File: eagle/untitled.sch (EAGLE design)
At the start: 29 parts, among them K1 AZ8-FORM-A, Q1 IRFZ24NPBF, U1 ATTINY85-20S, X1 MKDSN1,5/3-5,08, X2 MKDSN1,5/3-5,08

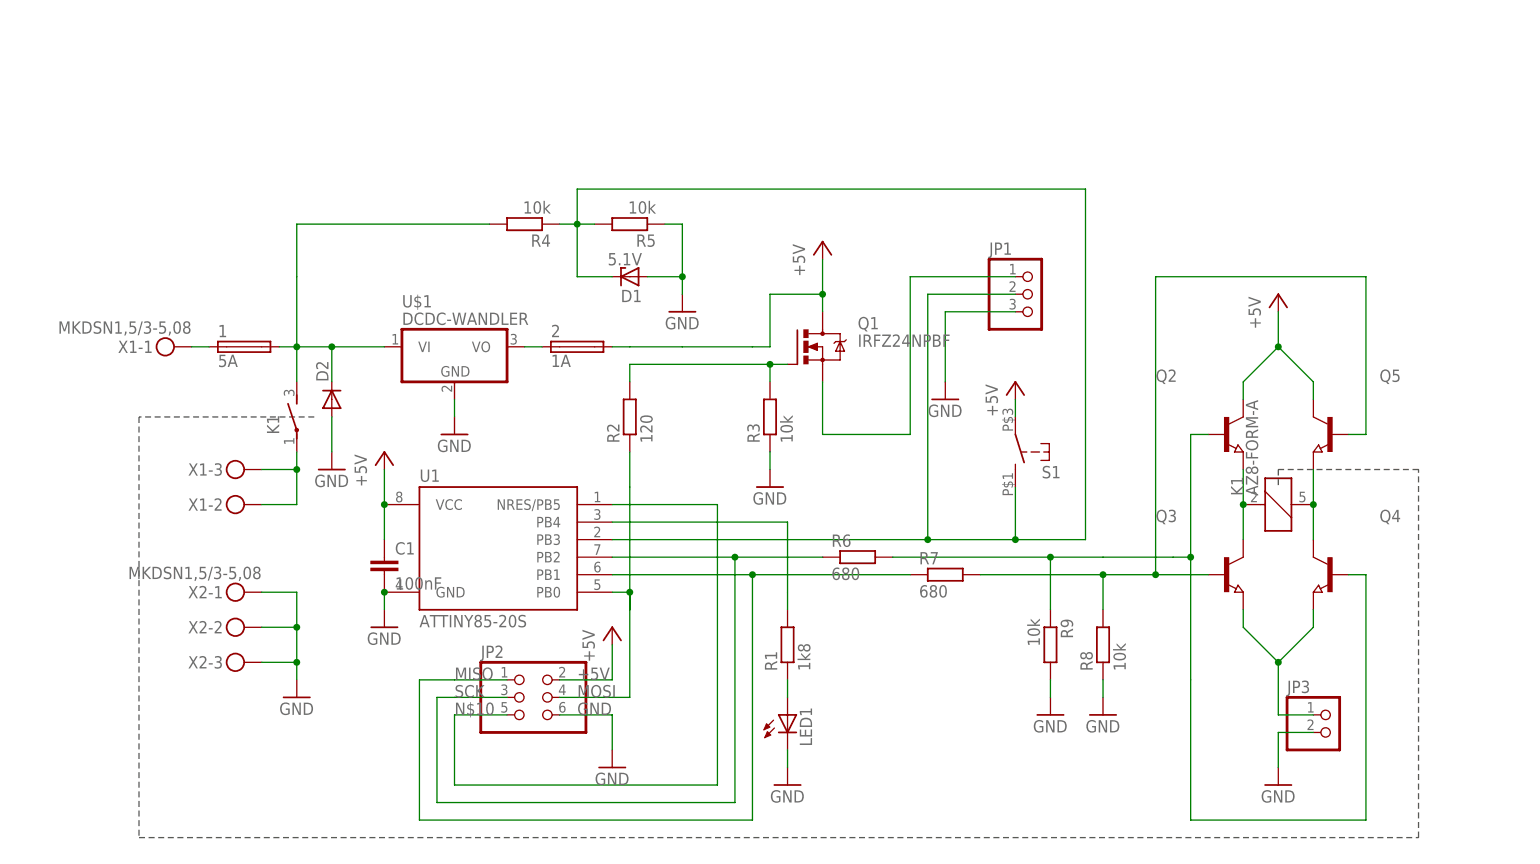
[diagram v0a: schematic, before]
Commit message: Added resistor for npn transistors
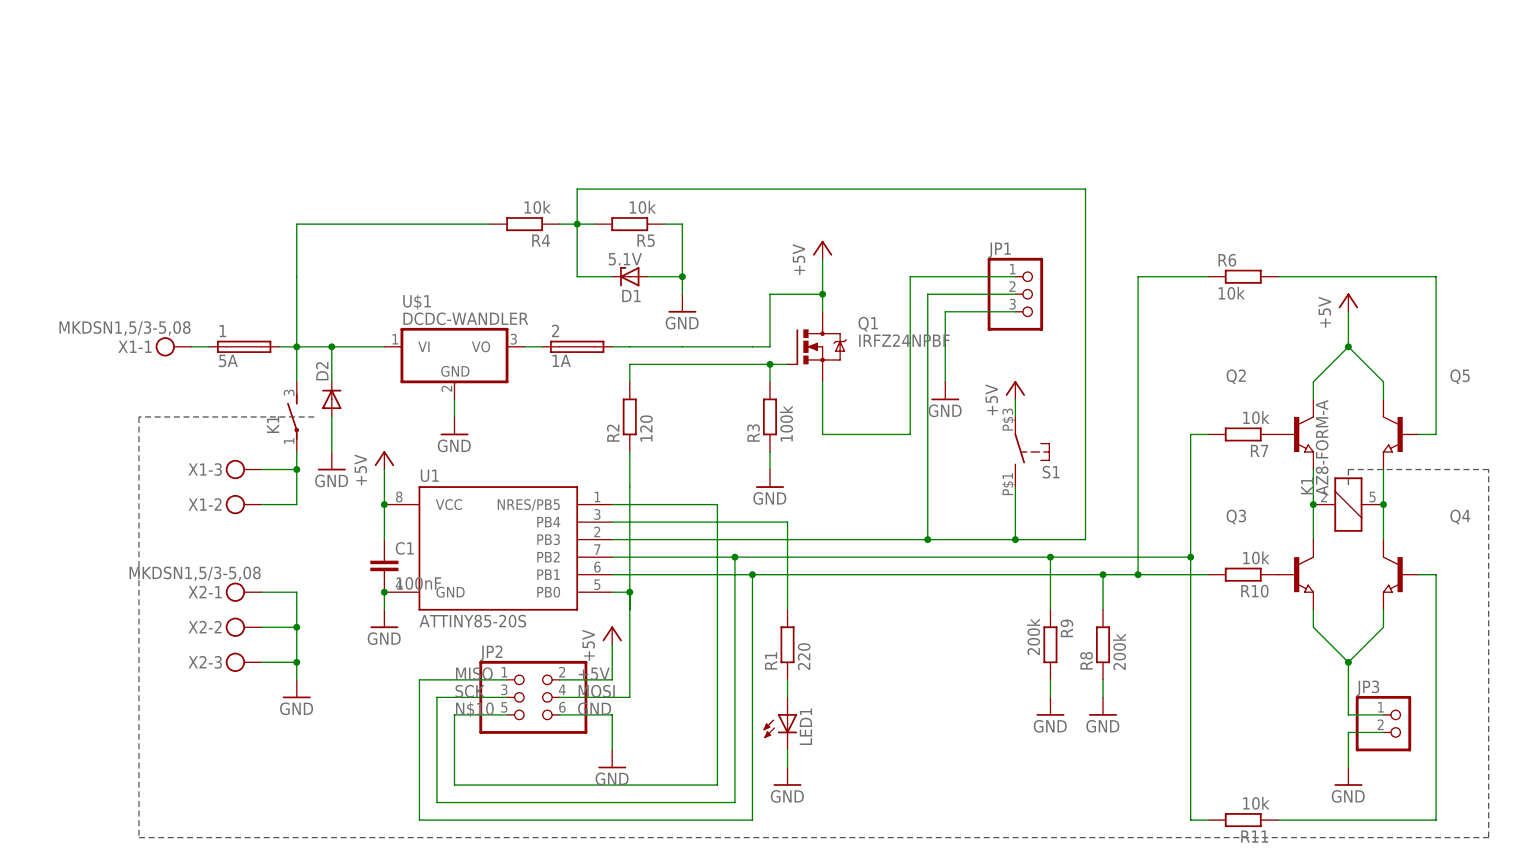
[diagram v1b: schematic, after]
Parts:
- added R10, R11: 10k, rcl:R-EU_R1206
- R1: value 1k8 -> 220
- R3: value 10k -> 100k
- R6, R7: value 680 -> 10k
- R8, R9: value 10k -> 200k
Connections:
- removed net N$16: Q3.B, Q5.B, R7.2, R8.2
- removed net N$17: Q2.B, Q4.B, R6.2, R9.1
- new net N$14: Q5.B, R6.2
- new net N$15: Q2.B, R7.1
- new net N$19: Q3.B, R10.1
- new net N$20: Q4.B, R11.1
- net MISO: now also R10.2, R6.1, R8.2; no longer R7.1
- net SCK: now also R11.2, R7.2, R9.1; no longer R6.1
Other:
- moved on the sheet: JP3, K1, Q2, Q3, Q4, Q5, R6, R7

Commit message: Pullup- reset & 2x voltage divider
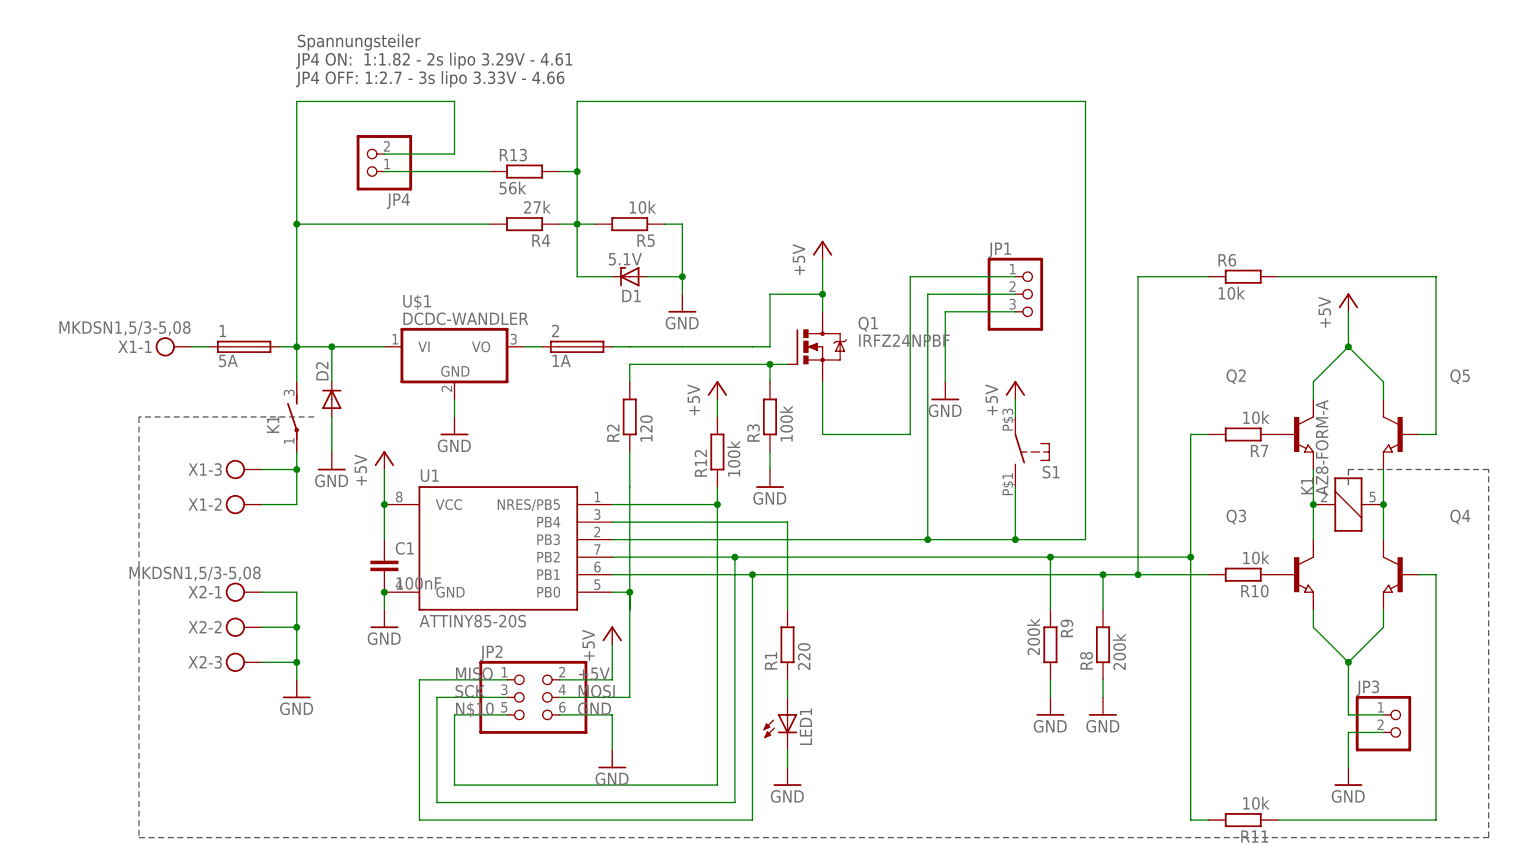
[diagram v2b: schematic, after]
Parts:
- added JP4: (no value), pinhead:PINHD-1X2
- added R12: 100k, rcl:R-EU_R1206
- added R13: 56k, rcl:R-EU_R1206
- R4: value 10k -> 27k
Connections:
- new net N$16: JP4.1, R13.1
- net +5V: now also R12.2
- net N$10: now also R12.1
- net N$2: now also JP4.2
- net RESET: now also R13.2
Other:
- note added: "Spannungsteiler JP4 ON: 1:1.82 - 2s lipo 3.29V - 4.61 JP4 OFF: 1:2.7 - 3s lipo 3.33V - 4.66"
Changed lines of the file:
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@@
 <part name="GND4" library="supply1" deviceset="GND" device=""/>
 <part name="JP1" library="pinhead" deviceset="PINHD-1X3" device=""/>
-<part name="R4" library="rcl" deviceset="R-EU_" device="R1206" value="10k"/>
+<part name="R4" library="rcl" deviceset="R-EU_" device="R1206" value="27k"/>
 <part name="R5" library="rcl" deviceset="R-EU_" device="R1206" value="10k"/>
 <part name="GND6" library="supply1" deviceset="GND" device=""/>
@@
 <part name="R10" library="rcl" deviceset="R-EU_" device="R1206" value="10k"/>
 <part name="R11" library="rcl" deviceset="R-EU_" device="R1206" value="10k"/>
+<part name="P+6" library="supply1" deviceset="+5V" device=""/>
+<part name="R12" library="rcl" deviceset="R-EU_" device="R1206" value="100k"/>
+<part name="JP4" library="pinhead" deviceset="PINHD-1X2" device=""/>
+<part name="R13" library="rcl" deviceset="R-EU_" device="R1206" value="56k"/>
 </parts>
 <sheets>
@@
 <wire x1="170.18" y1="71.12" x2="149.86" y2="71.12" width="0.1524" layer="97" style="shortdash"/>
 <wire x1="149.86" y1="71.12" x2="149.86" y2="68.58" width="0.1524" layer="97" style="shortdash"/>
+<text x="-2.54" y="127" size="1.778" layer="97">Spannungsteiler
+JP4 ON:  1:1.82 - 2s lipo 3.29V - 4.61
+JP4 OFF: 1:2.7 - 3s lipo 3.33V - 4.66</text>
 </plain>
 <instances>
@@
 <instance part="R10" gate="G$1" x="134.62" y="55.88" rot="R180"/>
 <instance part="R11" gate="G$1" x="134.62" y="20.32" rot="R180"/>
+<instance part="P+6" gate="1" x="58.42" y="83.82"/>
+<instance part="R12" gate="G$1" x="58.42" y="73.66" rot="R90"/>
+<instance part="JP4" gate="G$1" x="7.62" y="116.84" rot="R180"/>
+<instance part="R13" gate="G$1" x="30.48" y="114.3"/>
 </instances>
 <busses>
@@
 <pinref part="R4" gate="G$1" pin="2"/>
 <wire x1="-2.54" y1="106.68" x2="25.4" y2="106.68" width="0.1524" layer="91"/>
-<wire x1="-2.54" y1="99.06" x2="-2.54" y2="106.68" width="0.1524" layer="91"/>
 <pinref part="U$1" gate="G$1" pin="VI"/>
 <wire x1="-2.54" y1="88.9" x2="2.54" y2="88.9" width="0.1524" layer="91"/>
 <wire x1="2.54" y1="88.9" x2="10.16" y2="88.9" width="0.1524" layer="91"/>
-<wire x1="-2.54" y1="88.9" x2="-2.54" y2="99.06" width="0.1524" layer="91"/>
+<wire x1="-2.54" y1="88.9" x2="-2.54" y2="106.68" width="0.1524" layer="91"/>
 <junction x="-2.54" y="88.9"/>
 <pinref part="1" gate="G$1" pin="2"/>
@@
 <wire x1="2.54" y1="83.82" x2="2.54" y2="88.9" width="0.1524" layer="91"/>
 <junction x="2.54" y="88.9"/>
+<wire x1="-2.54" y1="106.68" x2="-2.54" y2="124.46" width="0.1524" layer="91"/>
+<junction x="-2.54" y="106.68"/>
+<wire x1="-2.54" y1="124.46" x2="20.32" y2="124.46" width="0.1524" layer="91"/>
+<wire x1="20.32" y1="124.46" x2="20.32" y2="116.84" width="0.1524" layer="91"/>
+<pinref part="JP4" gate="G$1" pin="2"/>
+<wire x1="20.32" y1="116.84" x2="10.16" y2="116.84" width="0.1524" layer="91"/>
 </segment>
 </net>
@@
 <wire x1="35.56" y1="106.68" x2="38.1" y2="106.68" width="0.1524" layer="91"/>
 <wire x1="38.1" y1="106.68" x2="40.64" y2="106.68" width="0.1524" layer="91"/>
-<wire x1="38.1" y1="106.68" x2="38.1" y2="111.76" width="0.1524" layer="91"/>
+<wire x1="38.1" y1="106.68" x2="38.1" y2="114.3" width="0.1524" layer="91"/>
 <junction x="38.1" y="106.68"/>
-<wire x1="38.1" y1="111.76" x2="111.76" y2="111.76" width="0.1524" layer="91"/>
+<wire x1="38.1" y1="114.3" x2="38.1" y2="124.46" width="0.1524" layer="91"/>
+<wire x1="38.1" y1="124.46" x2="111.76" y2="124.46" width="0.1524" layer="91"/>
 <pinref part="U1" gate="G$1" pin="PB3"/>
 <wire x1="43.18" y1="60.96" x2="88.9" y2="60.96" width="0.1524" layer="91"/>
 <wire x1="88.9" y1="60.96" x2="101.6" y2="60.96" width="0.1524" layer="91"/>
 <wire x1="101.6" y1="60.96" x2="111.76" y2="60.96" width="0.1524" layer="91"/>
-<wire x1="111.76" y1="60.96" x2="111.76" y2="111.76" width="0.1524" layer="91"/>
+<wire x1="111.76" y1="60.96" x2="111.76" y2="124.46" width="0.1524" layer="91"/>
 <pinref part="JP1" gate="A" pin="2"/>
 <wire x1="101.6" y1="96.52" x2="88.9" y2="96.52" width="0.1524" layer="91"/>
@@
 <wire x1="101.6" y1="68.58" x2="101.6" y2="60.96" width="0.1524" layer="91"/>
 <junction x="101.6" y="60.96"/>
+<pinref part="R13" gate="G$1" pin="2"/>
+<wire x1="38.1" y1="114.3" x2="35.56" y2="114.3" width="0.1524" layer="91"/>
+<junction x="38.1" y="114.3"/>
 </segment>
 </net>
@@
 <wire x1="66.04" y1="96.52" x2="73.66" y2="96.52" width="0.1524" layer="91"/>
 <junction x="73.66" y="96.52"/>
+</segment>
+<segment>
+<pinref part="P+6" gate="1" pin="+5V"/>
+<pinref part="R12" gate="G$1" pin="2"/>
+<wire x1="58.42" y1="81.28" x2="58.42" y2="78.74" width="0.1524" layer="91"/>
 </segment>
 </net>
@@
 <wire x1="20.32" y1="25.4" x2="58.42" y2="25.4" width="0.1524" layer="91"/>
 <label x="20.32" y="35.56" size="1.778" layer="95"/>
+<pinref part="R12" gate="G$1" pin="1"/>
+<wire x1="58.42" y1="68.58" x2="58.42" y2="66.04" width="0.1524" layer="91"/>
+<junction x="58.42" y="66.04"/>
 </segment>
 </net>
@@
 </segment>
 </net>
+<net name="N$16" class="0">
+<segment>
+<pinref part="R13" gate="G$1" pin="1"/>
+<pinref part="JP4" gate="G$1" pin="1"/>
+<wire x1="25.4" y1="114.3" x2="10.16" y2="114.3" width="0.1524" layer="91"/>
+</segment>
+</net>
 </nets>
 </sheet>
@@
 </schematic>
 </drawing>
+<compatibility>
+<note version="6.3" minversion="6.2.2" severity="warning">
+Since Version 6.2.2 text objects can contain more than one line,
+which will not be processed correctly with this version.
+</note>
+</compatibility>
 </eagle>

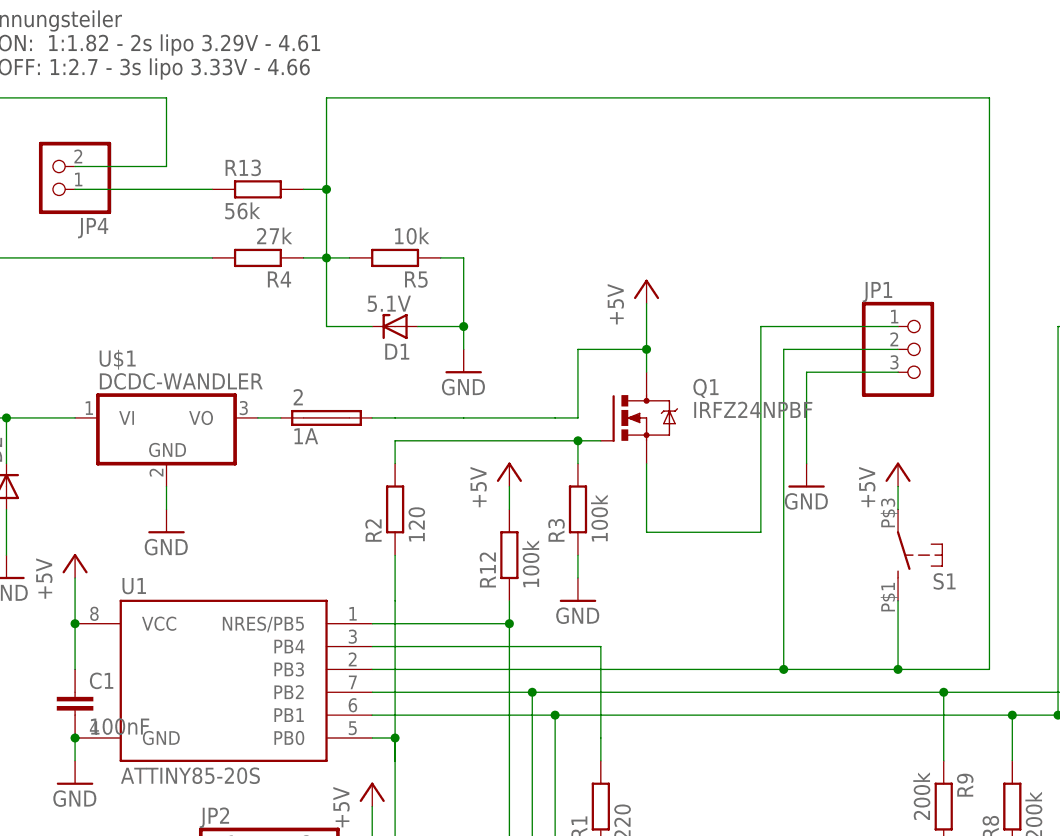
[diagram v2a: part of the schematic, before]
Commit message: Additional jumper for 2s and 3s lipo battery
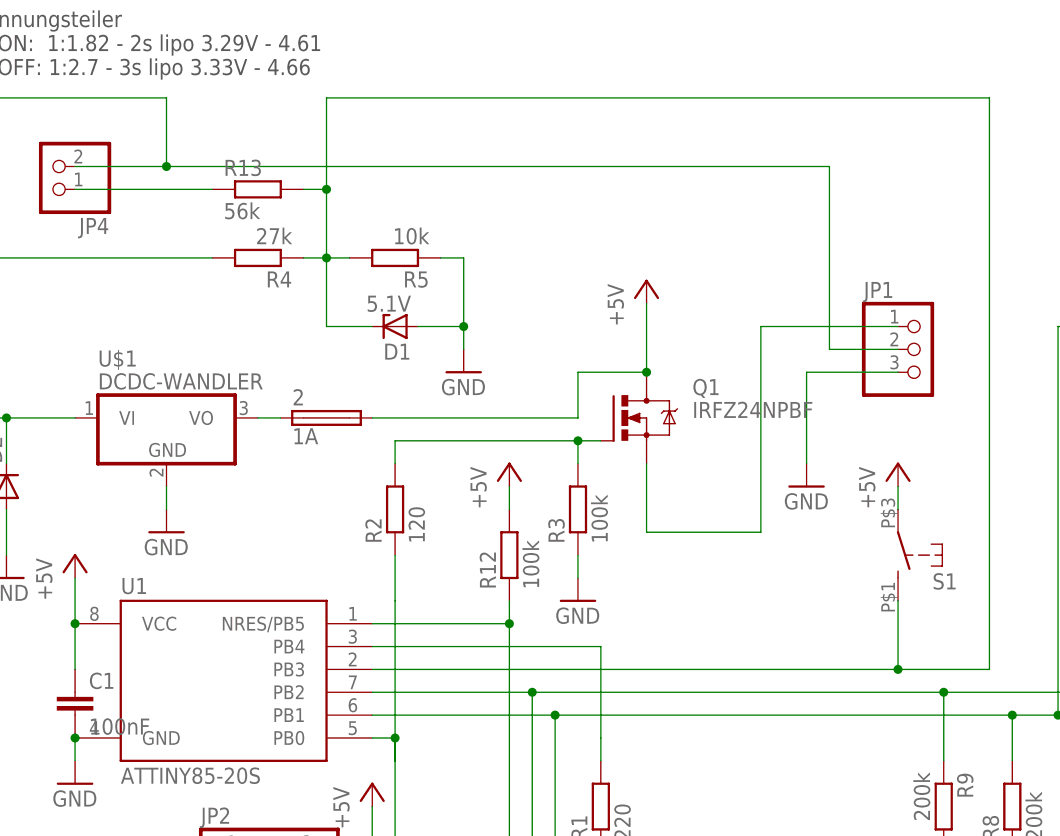
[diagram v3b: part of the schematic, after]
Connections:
- net N$2: now also JP1.2
- net RESET: no longer JP1.2
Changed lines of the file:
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@@
 <pinref part="JP4" gate="G$1" pin="2"/>
 <wire x1="20.32" y1="116.84" x2="10.16" y2="116.84" width="0.1524" layer="91"/>
+<junction x="20.32" y="116.84"/>
+<wire x1="20.32" y1="116.84" x2="93.98" y2="116.84" width="0.1524" layer="91"/>
+<wire x1="93.98" y1="116.84" x2="93.98" y2="96.52" width="0.1524" layer="91"/>
+<pinref part="JP1" gate="A" pin="2"/>
+<wire x1="93.98" y1="96.52" x2="101.6" y2="96.52" width="0.1524" layer="91"/>
 </segment>
 </net>
@@
 <wire x1="38.1" y1="124.46" x2="111.76" y2="124.46" width="0.1524" layer="91"/>
 <pinref part="U1" gate="G$1" pin="PB3"/>
-<wire x1="43.18" y1="60.96" x2="88.9" y2="60.96" width="0.1524" layer="91"/>
-<wire x1="88.9" y1="60.96" x2="101.6" y2="60.96" width="0.1524" layer="91"/>
+<wire x1="43.18" y1="60.96" x2="101.6" y2="60.96" width="0.1524" layer="91"/>
 <wire x1="101.6" y1="60.96" x2="111.76" y2="60.96" width="0.1524" layer="91"/>
 <wire x1="111.76" y1="60.96" x2="111.76" y2="124.46" width="0.1524" layer="91"/>
-<pinref part="JP1" gate="A" pin="2"/>
-<wire x1="101.6" y1="96.52" x2="88.9" y2="96.52" width="0.1524" layer="91"/>
-<wire x1="88.9" y1="96.52" x2="88.9" y2="60.96" width="0.1524" layer="91"/>
-<junction x="88.9" y="60.96"/>
 <wire x1="38.1" y1="106.68" x2="38.1" y2="99.06" width="0.1524" layer="91"/>
 <pinref part="D1" gate="G$1" pin="C"/>
@@
 </segment>
 <segment>
-<wire x1="43.18" y1="88.9" x2="45.72" y2="88.9" width="0.1524" layer="91"/>
-<wire x1="45.72" y1="88.9" x2="53.34" y2="88.9" width="0.1524" layer="91"/>
 <pinref part="Q1" gate="G$1" pin="D"/>
 <pinref part="2" gate="G$1" pin="2"/>
 <pinref part="P+1" gate="1" pin="+5V"/>
-<wire x1="73.66" y1="101.6" x2="73.66" y2="96.52" width="0.1524" layer="91"/>
-<wire x1="73.66" y1="96.52" x2="73.66" y2="93.98" width="0.1524" layer="91"/>
-<wire x1="53.34" y1="88.9" x2="63.5" y2="88.9" width="0.1524" layer="91"/>
-<wire x1="63.5" y1="88.9" x2="66.04" y2="88.9" width="0.1524" layer="91"/>
-<wire x1="66.04" y1="88.9" x2="66.04" y2="96.52" width="0.1524" layer="91"/>
-<wire x1="66.04" y1="96.52" x2="73.66" y2="96.52" width="0.1524" layer="91"/>
-<junction x="73.66" y="96.52"/>
-</segment>
-<segment>
+<wire x1="73.66" y1="101.6" x2="73.66" y2="93.98" width="0.1524" layer="91"/>
+<wire x1="43.18" y1="88.9" x2="66.04" y2="88.9" width="0.1524" layer="91"/>
+<wire x1="66.04" y1="88.9" x2="66.04" y2="93.98" width="0.1524" layer="91"/>
+<wire x1="66.04" y1="93.98" x2="73.66" y2="93.98" width="0.1524" layer="91"/>
+<junction x="73.66" y="93.98"/>
+</segment>
+<segment>
